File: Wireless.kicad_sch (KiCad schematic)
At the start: 12 parts, among them J3 APCI0108-P001A

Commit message: Replace v2 with updated RK3576_SBCv2 (Copy) Oct 2
- Update 18 sheets to Oct 2 15:37 local versions
- Keep cleaned layout: exclude .history/, Resources/, *.bak, *.lck,
  project.kicad_dru, .hs_rules.json, lowercase dup placeholders
  (fixtures/power), empty orphans (digital, mechanical, output,
  USBC_MCU, eMMC_UFS)
- Preserve LICENSE, README.md, .gitignore
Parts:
- added R284, R285: 2.2k, PCM_Resistor_SMD_AKL:R_0402_1005Metric, symbol Device:R_Small
- R177, R178, R184, R189, R253, R254: LCSC Part C114765 -> C106231; Mouser Part 603-RC0402FR-0722RL -> 603-RC0402FR-070RL
- R196: LCSC Part C106235 -> C60490; Mouser Part 603-RC0402FR-071KL -> 603-RC0402FR-0710KL
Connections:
- net VCC_3V3: now also R284.1, R285.1
- net I2C0_SCL_M1_TP_Wireless renamed I2C2_SCL_M0_USB_Wireless
- net I2C2_SCL_M0_USB_Wireless: now also R284.2
- net I2C0_SDA_M1_TP_Wireless renamed I2C2_SDA_M0_USB_Wireless
- net I2C2_SDA_M0_USB_Wireless: now also R285.2

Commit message: Relink hierarchical root: 18 sheets into RK3576 SBCv2 top level
Root was empty (no sheet boxes); all subsheets orphaned.
Rebuilt A1 top level linking RK3576, LPDDR5, Power, Ethernet,
HDMI, MIPI, PCIe, USB-A/C, Wireless, RTC, uSD, GPIO, OLED,
RP2350A, Connectors, Fixtures, DC_Power. block_diagrame kept
docs-only (unlinked, avoids double-instantiation). Lowercase
stub duplicates excluded. ERC: 1388 -> 770 violations.
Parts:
- removed J3: APCI0108-P001A, Datasheet_Footprints:APCI0108-P001A, symbol Datasheet_Symbols:APCI0108-P001A
- added J15: APCI0108-P001A, Datasheet_Footprints:APCI0108-P001A, symbol Datasheet_Symbols:APCI0108-P001A
- renumbered C354 to C248, C356 to C249, C361 to C250, C173 to C251, R184 to R176, R189 to R177, R253 to R178, R254 to R179, R178 to R180, R177 to R181, R196 to R182, R285 to R183, R284 to R184
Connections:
- net BT_REG_ON_L: now also J15.54 (~{BT_REG_ON})
- net BT_WAKE_DEV_L: now also J15.42 (~{BT_DEV_WAKE_L})
- net BT_WAKE_HOST_L: now also J15.20 (~{BT_HOST_WAKE_L})
- net GND: now also J15.1 (GND), J15.18 (GND), J15.33 (GND), J15.39 (GND), J15.45 (GND), J15.51 (GND), J15.57 (GND), J15.63 (GND), J15.67 (GND), J15.69 (GND), J15.7 (GND), J15.75 (GND)
- net I2C2_SCL_M0_USB_Wireless: now also J15.60 (I2C_SCL)
- net I2C2_SDA_M0_USB_Wireless: now also J15.58 (I2C_SDA)
- net RTC_32KOUT_WIFI: now also J15.50 (SUSCLK_32K)
- net SAI2_LRCK_M0: now also J15.10 (BT_PCM_SYNC)
- net SAI2_SCLK_M0: now also J15.8 (BT_PCM_CLK)
- net SAI2_SDI_M0: now also J15.12 (BT_PCM_OUT)
- net SAI2_SDO_M0: now also J15.14 (BT_PCM_IN)
- net UART4_CTSN_M1: now also J15.34 (BT_UART_RTS)
- net UART4_RTSN_M1: now also J15.36 (BT_UART_CTS)
- net UART4_RX_M1: now also J15.22 (BT_UART_TXD)
- net UART4_TX_M1: now also J15.32 (BT_UART_RXD)
- net VCC_3V3: now also J15.2 (VCC_3V3), J15.4 (VCC_3V3), J15.72 (VCC_3V3), J15.74 (VCC_3V3)
- net WIFI_REG_ON_L: now also J15.56 (~{WLAN_REG_ON})
- net WIFI_RESET_L: now also J15.23 (~{WLAN_RESET_N})
- net WIFI_WAKE_DEV_L: now also J15.40 (~{WLAN_DEV_WAKE_L})
- net WIFI_WAKE_HOST_L: now also J15.21 (~{WLAN_HOST_WAKE_L})
- net WIRELESS_ALERT_L: now also J15.62 (~{ALERT_N})
- net at R178.2: now also J15.17 (WLAN_SDIO_D2)
- net at R181.2: now also J15.11 (WLAN_SDIO_CMD)
- net at R176.2: now also J15.13 (WLAN_SDIO_D0)
- net at R177.2: now also J15.15 (WLAN_SDIO_D1)
- net at R179.2: now also J15.19 (WLAN_SDIO_D3)
- net at R180.2: now also J15.9 (WLAN_SDIO_CLK)

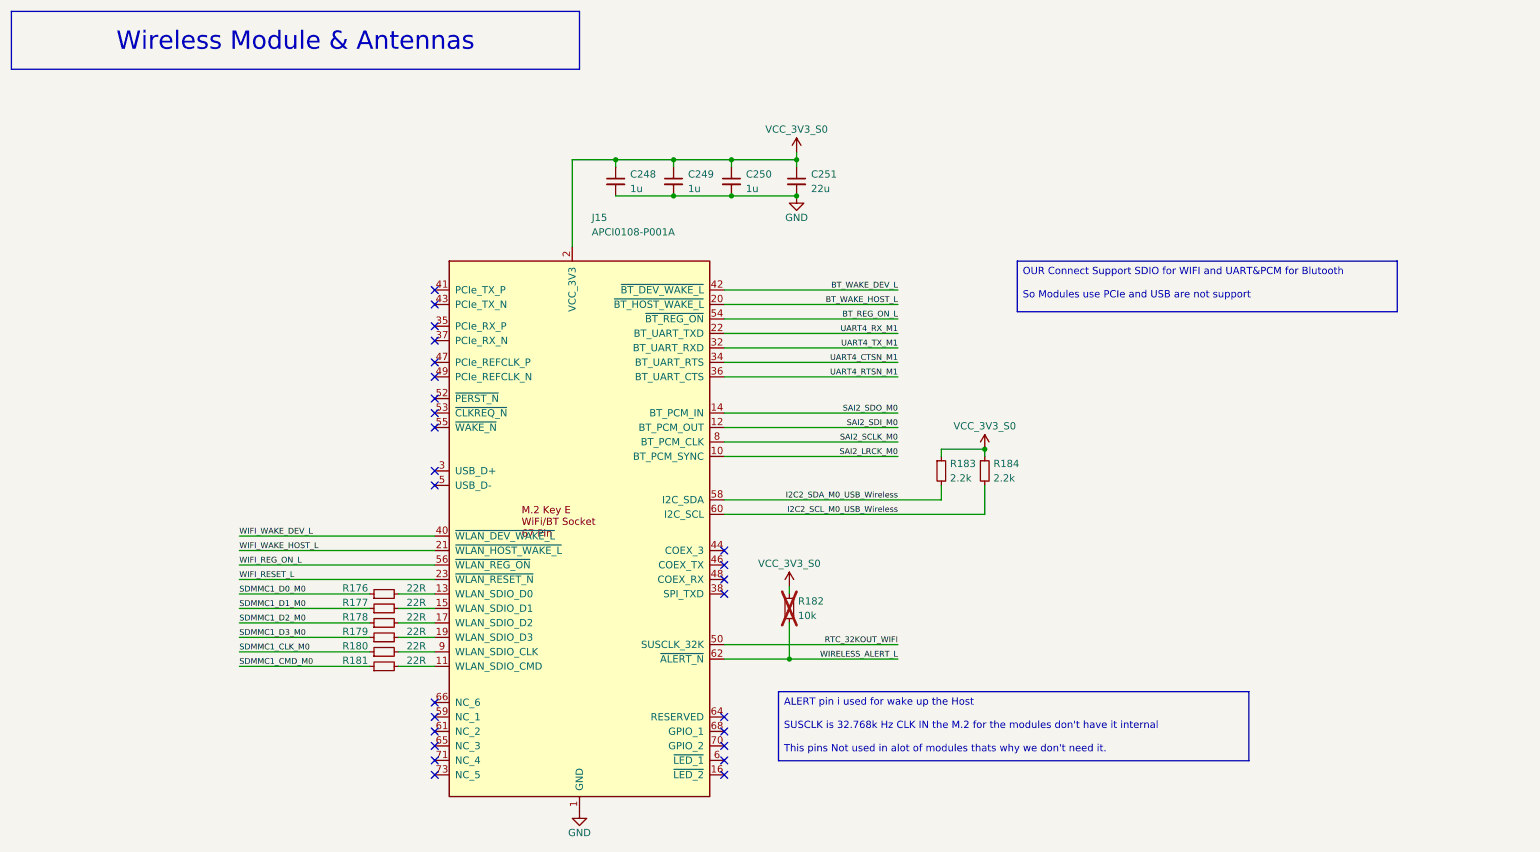
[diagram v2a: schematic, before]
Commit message: block diagrame with Hierarchical labels and NVMe SSD footprint
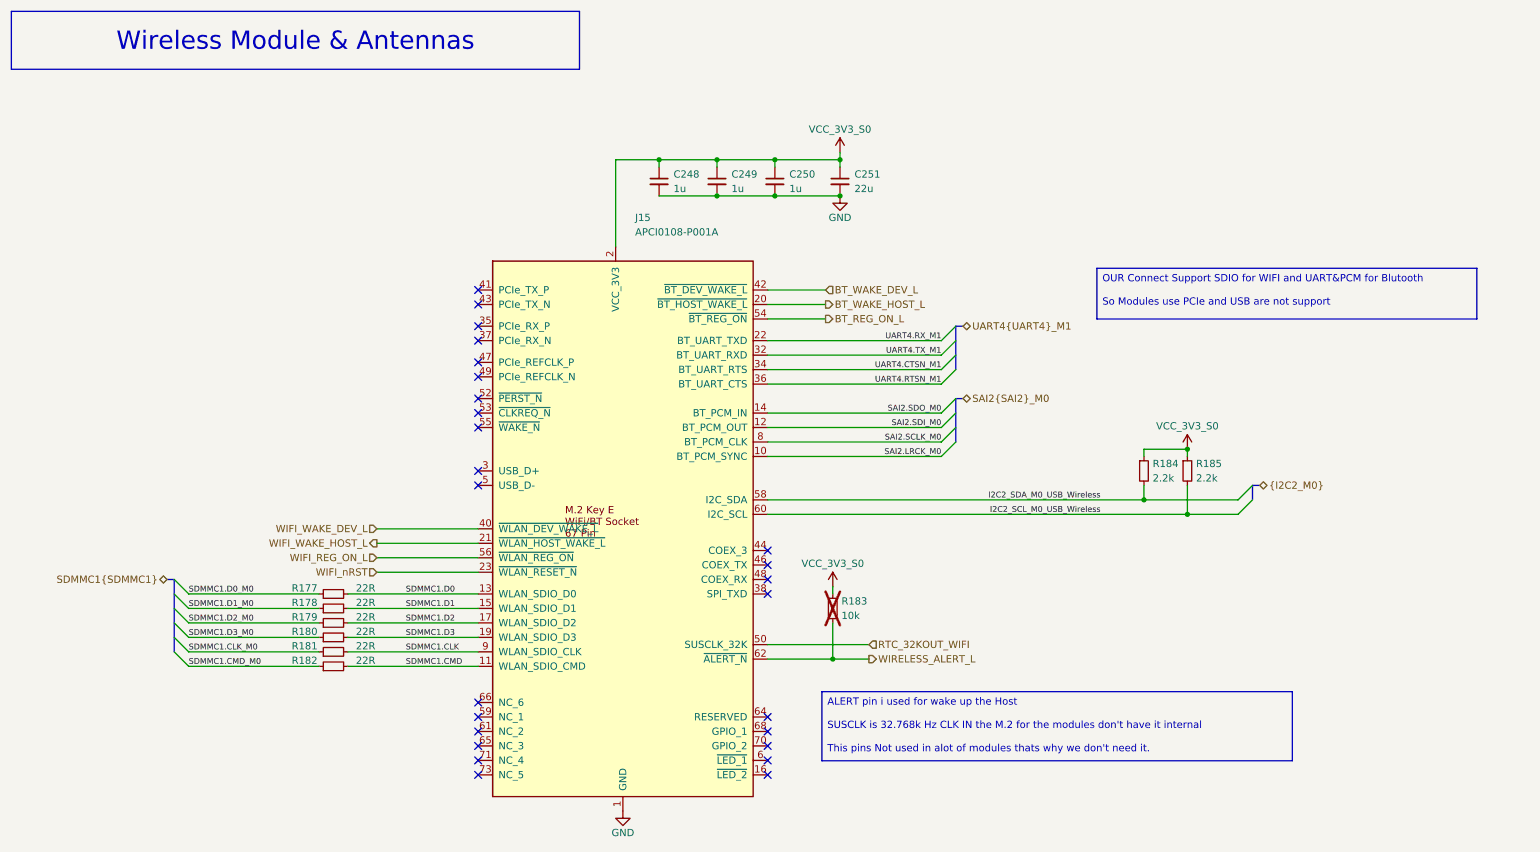
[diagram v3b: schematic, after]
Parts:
- renumbered R176 to R177, R177 to R178, R178 to R179, R179 to R180, R180 to R181, R181 to R182, R182 to R183, R183 to R184, R184 to R185
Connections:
- net SDMMC1.D2: now reaches J15.17 (WLAN_SDIO_D2), R179.2
- net SDMMC1.D1: now reaches J15.15 (WLAN_SDIO_D1), R178.2
- net SDMMC1.D3: now reaches J15.19 (WLAN_SDIO_D3), R180.2
- net SDMMC1.D0: now reaches J15.13 (WLAN_SDIO_D0), R177.2
- net SDMMC1.CLK: now reaches J15.9 (WLAN_SDIO_CLK), R181.2
- net SDMMC1.CMD: now reaches J15.11 (WLAN_SDIO_CMD), R182.2
- net SAI2_LRCK_M0 renamed SAI2.LRCK_M0
- net SAI2_SCLK_M0 renamed SAI2.SCLK_M0
- net SAI2_SDI_M0 renamed SAI2.SDI_M0
- net SAI2_SDO_M0 renamed SAI2.SDO_M0
- net SDMMC1_CLK_M0 renamed SDMMC1.CLK_M0
- net SDMMC1_CMD_M0 renamed SDMMC1.CMD_M0
- net SDMMC1_D0_M0 renamed SDMMC1.D0_M0
- net SDMMC1_D1_M0 renamed SDMMC1.D1_M0
- net SDMMC1_D2_M0 renamed SDMMC1.D2_M0
- net SDMMC1_D3_M0 renamed SDMMC1.D3_M0
- net UART4_CTSN_M1 renamed UART4.CTSN_M1
- net UART4_RTSN_M1 renamed UART4.RTSN_M1
- net UART4_RX_M1 renamed UART4.RX_M1
- net UART4_TX_M1 renamed UART4.TX_M1
- net WIFI_RESET_L renamed WIFI_nRST
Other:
- moved on the sheet: C248, C249, C250, C251, J15, R177, R178, R179, R180, R181, R182, R183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
